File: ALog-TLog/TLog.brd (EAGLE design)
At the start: 124.1 x 45.3 mm, 110 parts, among them IC1 ATMEGA644M, J6 5.5x2.1mm Barrel, Q11 MOSFET-NCH-BSS138, Q12 MOSFET_PCH-IRLML2244, Q5 MOSFET_PCH-IRLML2244, Q6 MOSFET_PCH-IRLML2244, Q7 MOSFET_PCH-IRLML2244, Q8 MOSFET-NCH-BSS138, Q9 MOSFET-NCH-BSS138, U2 FT231X-Q, U3 915MHz, U4 SX1509, X2 87832-14

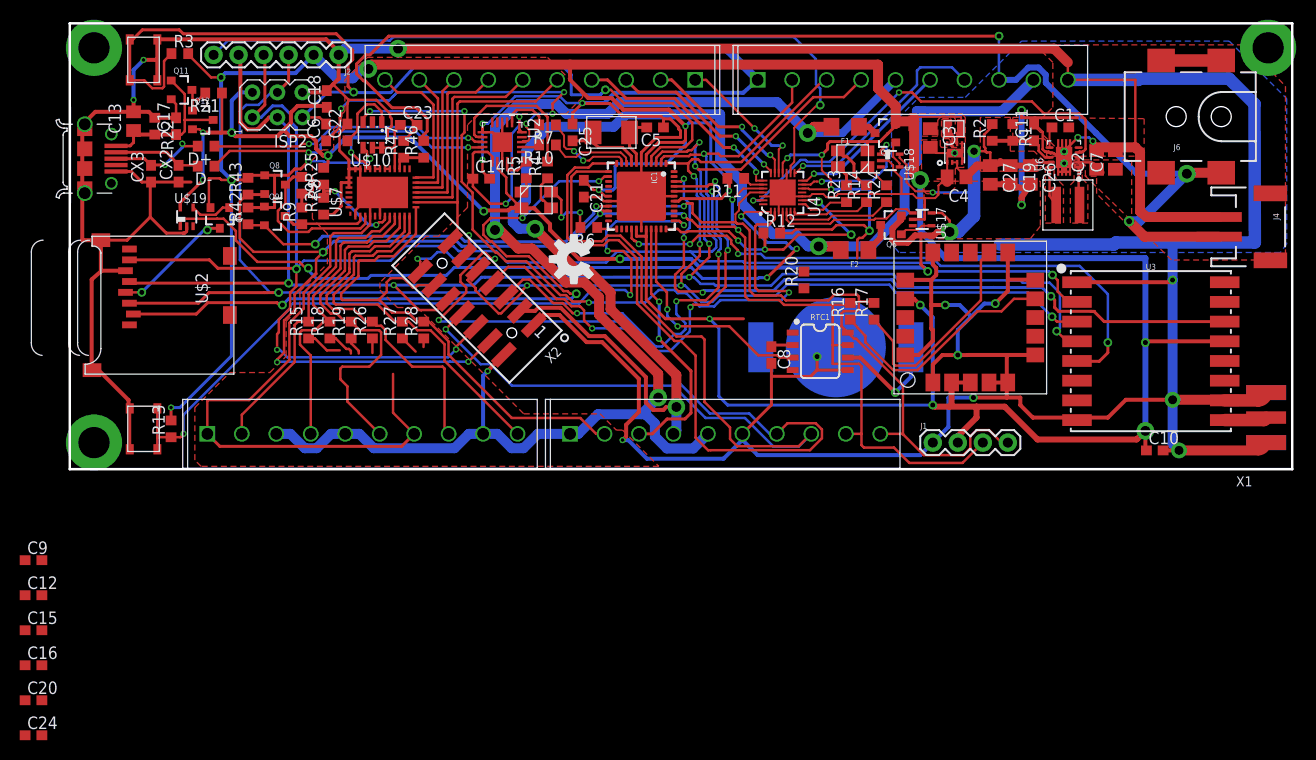
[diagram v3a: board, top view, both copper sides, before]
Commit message: Issue Fix Complete
Fixed issues: #9, #12, #8

Ready for review
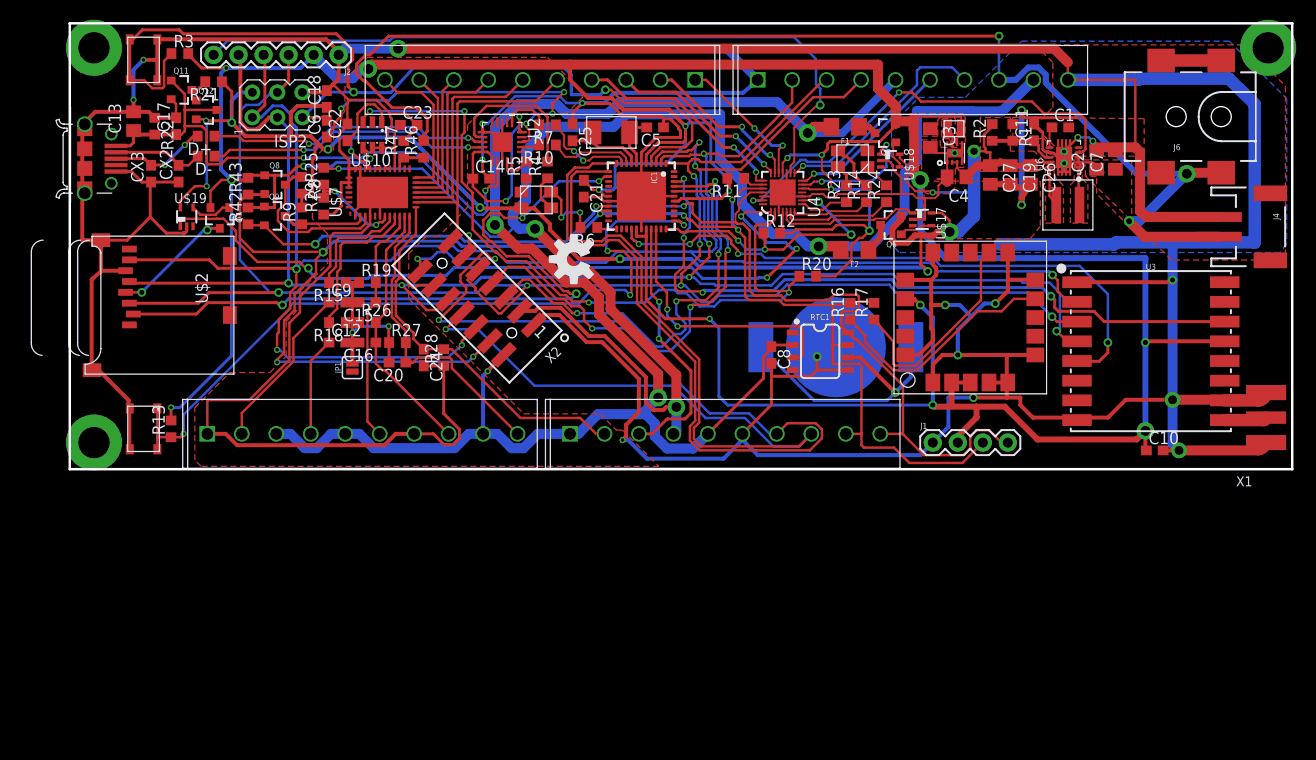
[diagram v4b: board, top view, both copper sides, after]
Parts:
- added JP1: JUMPER-SMT_2_NC_PASTE_SILK, SparkFun-Jumpers:SMT-JUMPER_2_NC_PASTE_SILK
- moved C24 55.1 mm to (36.1, 11.4), turned to 270 degrees
- moved C20 50.4 mm to (33.4, 10.9), turned to 180 degrees
- moved C15 47.5 mm to (30.4, 17.0), turned to 180 degrees
- moved C16 47.2 mm to (30.4, 13.0), turned to 180 degrees
- moved C9 40.5 mm to (27.3, 17.0)
- moved C12 40.1 mm to (27.3, 13.0)
- moved R15 5.64 mm to (27.3, 19.1), turned to 180 degrees
- moved R19 5.10 mm to (30.4, 19.1), turned to 0 degrees
- moved R28 3.45 mm to (38.1, 11.4)
- moved R27 1.37 mm to (33.4, 13.0), turned to 0 degrees
- moved R21 1.14 mm to (14.7, 39.4)
- moved Q12 1.09 mm to (14.0, 36.6)
- moved R18 1.08 mm to (27.3, 15.0), turned to 180 degrees
- moved D+ 1.02 mm to (14.0, 33.9)
- moved D- 1.02 mm to (14.0, 31.9)
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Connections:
- removed net 5V_EXT: R25.2
- new net THERM_GND: C12.2, C15.2, C16.2, C20.2, C9.2, JP1.2, R15.1, R18.1, R19.1, R26.1, R27.1
- net 5V: no longer U2.12
- net EXT_5V: now also R25.2
- net GND: now also JP1.1; no longer C12.2, C15.2, C16.2, C20.2, C9.2, R15.1, R18.1, R19.1, R26.1, R27.1
- net VUSB: now also U2.12
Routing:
- net VUSB: track 17.7 -> 61.1 mm, vias 0 -> 2
- net EXT_5V: track 137.4 -> 160.5 mm, vias 3 -> 4
- net THERM_GND: track 0.00 -> 21.3 mm, vias 0 -> 2
- net N$31: track 11.6 -> 27.8 mm
- net ADC5: track 55.1 -> 42.4 mm
- net ADC2: track 36.8 -> 24.3 mm
- net EXT_3.3V: track 149.8 -> 161.3 mm
- net ADC3: track 36.2 -> 26.5 mm
- net ADC4: track 39.2 -> 31.6 mm
- net GND: track 822.7 -> 817.1 mm
- net RTC_INT: track 23.8 -> 27.3 mm
- net ADC1: track 31.1 -> 27.6 mm
- net 5V: track 178.4 -> 176.1 mm
- net REF_CTRL: track 73.4 -> 75.5 mm
- net TX_EXT: track 96.2 -> 97.3 mm
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
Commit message: Presumptive Mrk 1.2
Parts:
- C12, C15, C16, C20, C24, C8, C9: value (none) -> 0.1uF
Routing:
- net GND: track 817.1 -> 818.8 mm

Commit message: Added Gerbers and Minor Edits
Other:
- outline, holes or cut-outs redrawn

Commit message: Updated Gerbers, ready for final review
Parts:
- Q8, Q9: value MOSFET-NCH-BSS138 -> 310mA/60V/1.6Ω; device bschulz:SOT23-3 -> bschulz:SOT323
- moved Q11 0.13 mm to (11.6, 38.6)
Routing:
- net GND: track 818.7 -> 834.6 mm
- net DTR: track 35.2 -> 35.8 mm
- net EXT_3.3V: track 161.3 -> 161.9 mm

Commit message: Updated gerbers for Mrk 1.2, added pick and place info
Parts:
- R21, R22: device rcl:R0603 -> bschulz_passives:R0603
- U$1: value CRYSTAL_5X3.2_2LEAD -> CRYSTAL_5X3.2_2LEAD8MHZ
- U$17, U$18, U$19: value MIC842 -> MIC842H
- U3: device SparkFun-RF:RFM69HCW-XXXS2 -> bschulz:RFM69HCW-XXXS2
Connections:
- new net RADIO_RESET: IC1.25, U3.6
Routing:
- net RADIO_RESET: track 0.00 -> 60.9 mm, vias 0 -> 2
- net TX_EXT: track 97.3 -> 95.8 mm
- net RX_EXT: track 99.6 -> 98.1 mm
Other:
- board text added: "TLog v1.0.1 ---------------------- Open-source scientific data logger ---------------------- Made in Minnesota"
- board text removed: "TLog v1.0.0 ---------------------- Open-source scientific data logger ---------------------- Made in Minnesota"
